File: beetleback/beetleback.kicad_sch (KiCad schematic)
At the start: 22 parts, among them J1 Conn_01x05_Female, J3 motor_pad_1, J4 motor_pad_2, Q1 IRF7351TRPBF, Q2 IRF7351TRPBF, U1 ATtiny13A-SS, U2 DRV8701P

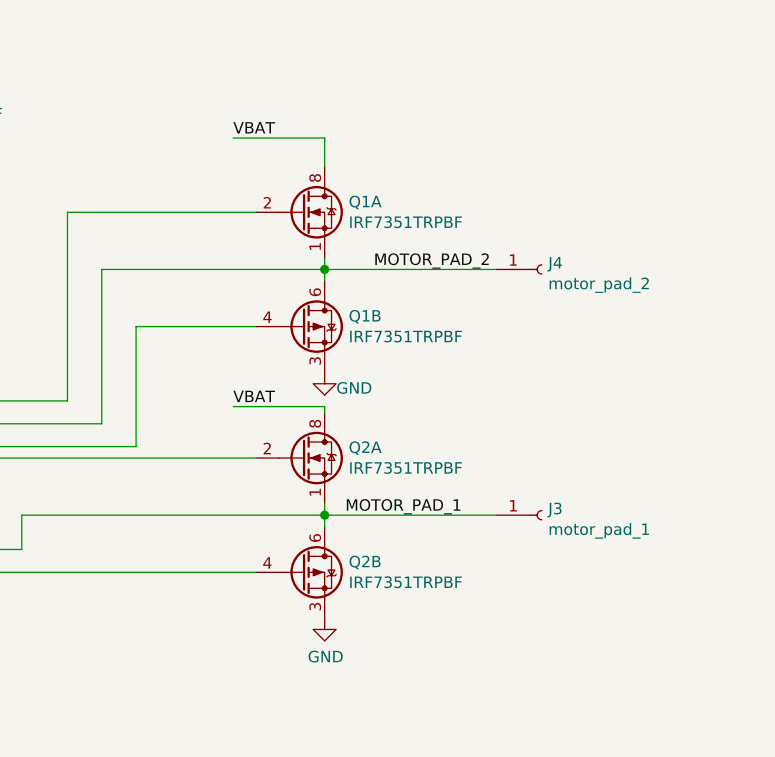
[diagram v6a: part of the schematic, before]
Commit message: Correct schematic booboo: use n-channel mosfets instead of a mixture
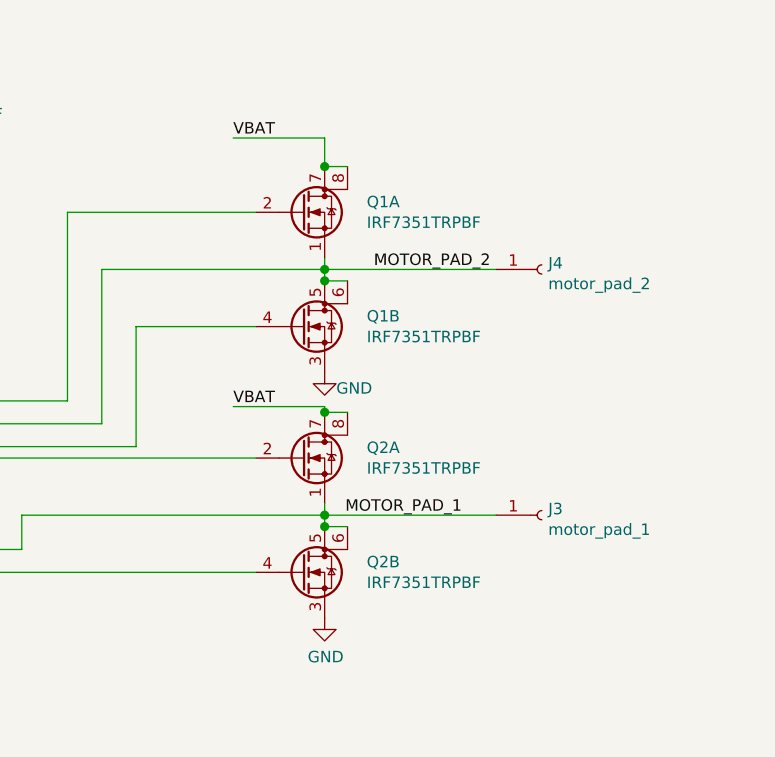
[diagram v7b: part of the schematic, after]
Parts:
- removed Q1, Q2: IRF7351TRPBF, Package_SO:SOIC-8_3.9x4.9mm_P1.27mm, symbol Transistor_FET:IRF7343PBF
- added Q1, Q2: IRF7351TRPBF, Package_SO:SOIC-8_3.9x4.9mm_P1.27mm, symbol Device:Q_Dual_NMOS_S1G1S2G2D2D2D1D1
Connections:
- net GH1: now also Q1.2 (G)
- net GH2: now also Q2.2 (G)
- net GL1: now also Q1.4 (G)
- net GL2: now also Q2.4 (G)
- net GND: now also Q1.3 (S), Q2.3 (S)
- net MOTOR_PAD_1: now also Q2.1 (S), Q2.5 (D), Q2.6 (D)
- net MOTOR_PAD_2: now also Q1.1 (S), Q1.5 (D), Q1.6 (D)
- net VBAT: now also Q1.7 (D), Q1.8 (D), Q2.7 (D), Q2.8 (D)
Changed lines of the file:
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@@
   (junction (at 172.72 87.63) (diameter 1.016) (color 0 0 0 0))
   (junction (at 196.85 103.505) (diameter 1.016) (color 0 0 0 0))
+  (junction (at 244.475 97.155) (diameter 1.016) (color 0 0 0 0))
   (junction (at 244.475 108.585) (diameter 1.016) (color 0 0 0 0))
+  (junction (at 244.475 109.855) (diameter 1.016) (color 0 0 0 0))
+  (junction (at 244.475 124.46) (diameter 1.016) (color 0 0 0 0))
   (junction (at 244.475 135.89) (diameter 1.016) (color 0 0 0 0))
+  (junction (at 244.475 137.16) (diameter 1.016) (color 0 0 0 0))
+  (no_connect (at 27.94 50.8))
   (no_connect (at 182.88 118.745))
-  (no_connect (at 27.94 50.8))
   (no_connect (at 182.88 147.955))
   (no_connect (at 178.435 66.04))
@@
     (stroke (width 0) (type solid) (color 0 0 0 0))
   )
+  (wire (pts (xy 244.475 97.155) (xy 247.015 97.155))
+    (stroke (width 0) (type solid) (color 0 0 0 0))
+  )
   (wire (pts (xy 244.475 107.315) (xy 244.475 108.585))
     (stroke (width 0) (type solid) (color 0 0 0 0))
@@
     (stroke (width 0) (type solid) (color 0 0 0 0))
   )
+  (wire (pts (xy 244.475 109.855) (xy 247.015 109.855))
+    (stroke (width 0) (type solid) (color 0 0 0 0))
+  )
   (wire (pts (xy 244.475 123.825) (xy 244.475 124.46))
     (stroke (width 0) (type solid) (color 0 0 0 0))
   )
+  (wire (pts (xy 244.475 124.46) (xy 247.015 124.46))
+    (stroke (width 0) (type solid) (color 0 0 0 0))
+  )
   (wire (pts (xy 244.475 134.62) (xy 244.475 135.89))
     (stroke (width 0) (type solid) (color 0 0 0 0))
@@
   )
   (wire (pts (xy 244.475 135.89) (xy 263.525 135.89))
+    (stroke (width 0) (type solid) (color 0 0 0 0))
+  )
+  (wire (pts (xy 244.475 137.16) (xy 247.015 137.16))
     (stroke (width 0) (type solid) (color 0 0 0 0))
   )
@@
     )
   )
-  (symbol (lib_id "Transistor_FET:IRF7343PBF") (at 241.935 102.235 0) (unit 1)
-    (in_bom yes) (on_board yes)
-    (property "Reference" "Q1" (id 0) (at 247.1421 101.0856 0)
-      (effects (font (size 1.27 1.27)) (justify left))
-    )
-    (property "Value" "IRF7351TRPBF" (id 1) (at 247.142 103.384 0)
-      (effects (font (size 1.27 1.27)) (justify left))
-    )
-    (property "Footprint" "Package_SO:SOIC-8_3.9x4.9mm_P1.27mm" (id 2) (at 247.015 104.14 0)
-      (effects (font (size 1.27 1.27)) (justify left) hide)
-    )
-    (property "Datasheet" "http://www.irf.com/product-info/datasheets/data/irf7343ipbf.pdf" (id 3) (at 244.475 102.235 0)
-      (effects (font (size 1.27 1.27)) (justify left) hide)
+  (symbol (lib_id "Graphic:Logo_Open_Hardware_Small") (at 186.69 23.495 0) (unit 1)
+    (in_bom yes) (on_board yes)
+    (property "Reference" "#LOGO1" (id 0) (at 186.69 16.51 0)
+      (effects (font (size 1.27 1.27)) hide)
+    )
+    (property "Value" "Logo_Open_Hardware_Small" (id 1) (at 186.69 29.21 0)
+      (effects (font (size 1.27 1.27)) hide)
+    )
+    (property "Footprint" "beetleback:bbb_logo" (id 2) (at 186.69 23.495 0)
+      (effects (font (size 1.27 1.27)) hide)
+    )
+    (property "Datasheet" "~" (id 3) (at 186.69 23.495 0)
+      (effects (font (size 1.27 1.27)) hide)
+    )
+  )
+  (symbol (lib_id "Device:Q_Dual_NMOS_S1G1S2G2D2D2D1D1") (at 241.935 102.235 0) (unit 1)
+    (in_bom yes) (on_board yes)
+    (property "Reference" "Q1" (id 0) (at 249.1487 101.0856 0)
+      (effects (font (size 1.27 1.27)) (justify left))
+    )
+    (property "Value" "IRF7351TRPBF" (id 1) (at 249.149 103.384 0)
+      (effects (font (size 1.27 1.27)) (justify left))
+    )
+    (property "Footprint" "Package_SO:SOIC-8_3.9x4.9mm_P1.27mm" (id 2) (at 247.015 102.235 0)
+      (effects (font (size 1.27 1.27)) hide)
+    )
+    (property "Datasheet" "~" (id 3) (at 247.015 102.235 0)
+      (effects (font (size 1.27 1.27)) hide)
     )
     (property "LCSC" "C68403" (id 4) (at 241.935 102.235 0)
@@
     )
   )
-  (symbol (lib_id "Transistor_FET:IRF7343PBF") (at 241.935 114.935 0) (unit 2)
-    (in_bom yes) (on_board yes)
-    (property "Reference" "Q1" (id 0) (at 247.1421 113.7856 0)
-      (effects (font (size 1.27 1.27)) (justify left))
-    )
-    (property "Value" "IRF7351TRPBF" (id 1) (at 247.1421 116.0843 0)
-      (effects (font (size 1.27 1.27)) (justify left))
-    )
-    (property "Footprint" "Package_SO:SOIC-8_3.9x4.9mm_P1.27mm" (id 2) (at 247.015 116.84 0)
-      (effects (font (size 1.27 1.27)) (justify left) hide)
-    )
-    (property "Datasheet" "http://www.irf.com/product-info/datasheets/data/irf7343ipbf.pdf" (id 3) (at 244.475 114.935 0)
-      (effects (font (size 1.27 1.27)) (justify left) hide)
-    )
-    (property "LCSC" "C68403" (id 4) (at 241.935 114.935 0)
-      (effects (font (size 1.27 1.27)) hide)
-    )
-  )
-  (symbol (lib_id "Transistor_FET:IRF7343PBF") (at 241.935 129.54 0) (unit 1)
-    (in_bom yes) (on_board yes)
-    (property "Reference" "Q2" (id 0) (at 247.1421 128.3906 0)
-      (effects (font (size 1.27 1.27)) (justify left))
-    )
-    (property "Value" "IRF7351TRPBF" (id 1) (at 247.142 130.689 0)
-      (effects (font (size 1.27 1.27)) (justify left))
-    )
-    (property "Footprint" "Package_SO:SOIC-8_3.9x4.9mm_P1.27mm" (id 2) (at 247.015 131.445 0)
-      (effects (font (size 1.27 1.27)) (justify left) hide)
-    )
-    (property "Datasheet" "http://www.irf.com/product-info/datasheets/data/irf7343ipbf.pdf" (id 3) (at 244.475 129.54 0)
-      (effects (font (size 1.27 1.27)) (justify left) hide)
+  (symbol (lib_id "Device:Q_Dual_NMOS_S1G1S2G2D2D2D1D1") (at 241.935 114.935 0) (unit 2)
+    (in_bom yes) (on_board yes)
+    (property "Reference" "Q1" (id 0) (at 249.1487 113.7856 0)
+      (effects (font (size 1.27 1.27)) (justify left))
+    )
+    (property "Value" "IRF7351TRPBF" (id 1) (at 249.149 116.084 0)
+      (effects (font (size 1.27 1.27)) (justify left))
+    )
+    (property "Footprint" "Package_SO:SOIC-8_3.9x4.9mm_P1.27mm" (id 2) (at 247.015 114.935 0)
+      (effects (font (size 1.27 1.27)) hide)
+    )
+    (property "Datasheet" "~" (id 3) (at 247.015 114.935 0)
+      (effects (font (size 1.27 1.27)) hide)
+    )
+  )
+  (symbol (lib_id "Device:Q_Dual_NMOS_S1G1S2G2D2D2D1D1") (at 241.935 129.54 0) (unit 1)
+    (in_bom yes) (on_board yes)
+    (property "Reference" "Q2" (id 0) (at 249.1487 128.3906 0)
+      (effects (font (size 1.27 1.27)) (justify left))
+    )
+    (property "Value" "IRF7351TRPBF" (id 1) (at 249.149 130.689 0)
+      (effects (font (size 1.27 1.27)) (justify left))
+    )
+    (property "Footprint" "Package_SO:SOIC-8_3.9x4.9mm_P1.27mm" (id 2) (at 247.015 129.54 0)
+      (effects (font (size 1.27 1.27)) hide)
+    )
+    (property "Datasheet" "~" (id 3) (at 247.015 129.54 0)
+      (effects (font (size 1.27 1.27)) hide)
     )
     (property "LCSC" "C68403" (id 4) (at 241.935 129.54 0)
@@
     )
   )
-  (symbol (lib_id "Transistor_FET:IRF7343PBF") (at 241.935 142.24 0) (unit 2)
-    (in_bom yes) (on_board yes)
-    (property "Reference" "Q2" (id 0) (at 247.1421 141.0906 0)
-      (effects (font (size 1.27 1.27)) (justify left))
-    )
-    (property "Value" "IRF7351TRPBF" (id 1) (at 247.1421 143.3893 0)
-      (effects (font (size 1.27 1.27)) (justify left))
-    )
-    (property "Footprint" "Package_SO:SOIC-8_3.9x4.9mm_P1.27mm" (id 2) (at 247.015 144.145 0)
-      (effects (font (size 1.27 1.27)) (justify left) hide)
-    )
-    (property "Datasheet" "http://www.irf.com/product-info/datasheets/data/irf7343ipbf.pdf" (id 3) (at 244.475 142.24 0)
-      (effects (font (size 1.27 1.27)) (justify left) hide)
-    )
-    (property "LCSC" "C68403" (id 4) (at 241.935 142.24 0)
-      (effects (font (size 1.27 1.27)) hide)
-    )
-  )
-  (symbol (lib_id "Graphic:Logo_Open_Hardware_Small") (at 186.69 23.495 0) (unit 1)
-    (in_bom yes) (on_board yes)
-    (property "Reference" "#LOGO1" (id 0) (at 186.69 16.51 0)
-      (effects (font (size 1.27 1.27)) hide)
-    )
-    (property "Value" "Logo_Open_Hardware_Small" (id 1) (at 186.69 29.21 0)
-      (effects (font (size 1.27 1.27)) hide)
-    )
-    (property "Footprint" "beetleback:bbb_logo" (id 2) (at 186.69 23.495 0)
-      (effects (font (size 1.27 1.27)) hide)
-    )
-    (property "Datasheet" "~" (id 3) (at 186.69 23.495 0)
+  (symbol (lib_id "Device:Q_Dual_NMOS_S1G1S2G2D2D2D1D1") (at 241.935 142.24 0) (unit 2)
+    (in_bom yes) (on_board yes)
+    (property "Reference" "Q2" (id 0) (at 249.1487 141.0906 0)
+      (effects (font (size 1.27 1.27)) (justify left))
+    )
+    (property "Value" "IRF7351TRPBF" (id 1) (at 249.149 143.389 0)
+      (effects (font (size 1.27 1.27)) (justify left))
+    )
+    (property "Footprint" "Package_SO:SOIC-8_3.9x4.9mm_P1.27mm" (id 2) (at 247.015 142.24 0)
+      (effects (font (size 1.27 1.27)) hide)
+    )
+    (property "Datasheet" "~" (id 3) (at 247.015 142.24 0)
       (effects (font (size 1.27 1.27)) hide)
     )
@@
       (reference "J4") (unit 1) (value "motor_pad_2") (footprint "beetleback:bbb_motorpin")
     )
-    (path "/0f33e45a-ef24-4ac4-83eb-7cf104015784"
+    (path "/a69a273c-4e3e-46dc-8062-8d9f361d07d3"
       (reference "Q1") (unit 1) (value "IRF7351TRPBF") (footprint "Package_SO:SOIC-8_3.9x4.9mm_P1.27mm")
     )
-    (path "/bf41a1ad-5460-44cc-b329-1c158f60a46d"
+    (path "/86cb0b69-ddbd-42cc-8e88-2d4ebc15451c"
       (reference "Q1") (unit 2) (value "IRF7351TRPBF") (footprint "Package_SO:SOIC-8_3.9x4.9mm_P1.27mm")
     )
-    (path "/40ea8a05-4afc-4962-9870-9910f719101e"
+    (path "/d094f7e5-7051-4491-9470-d138e254b828"
       (reference "Q2") (unit 1) (value "IRF7351TRPBF") (footprint "Package_SO:SOIC-8_3.9x4.9mm_P1.27mm")
     )
-    (path "/23f89606-4f0f-4a94-8596-a6b3669b94fd"
+    (path "/fdf323e3-1e06-45a9-b347-9010497d9e39"
       (reference "Q2") (unit 2) (value "IRF7351TRPBF") (footprint "Package_SO:SOIC-8_3.9x4.9mm_P1.27mm")
     )

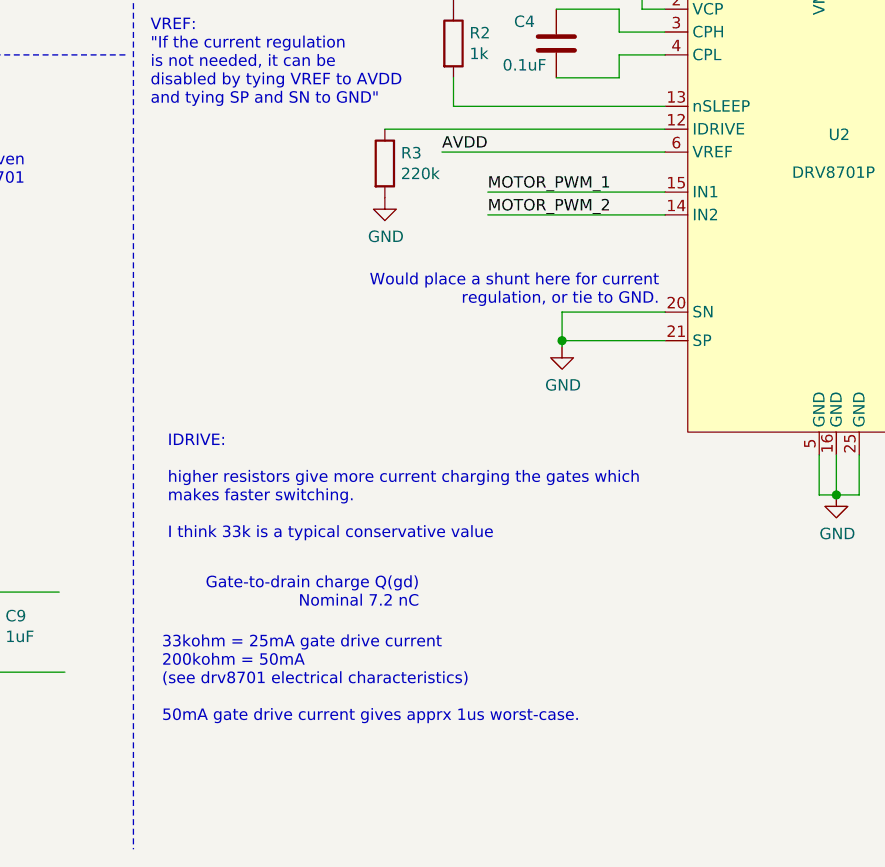
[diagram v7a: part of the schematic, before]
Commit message: more copper under fets, r3 dnp 0603
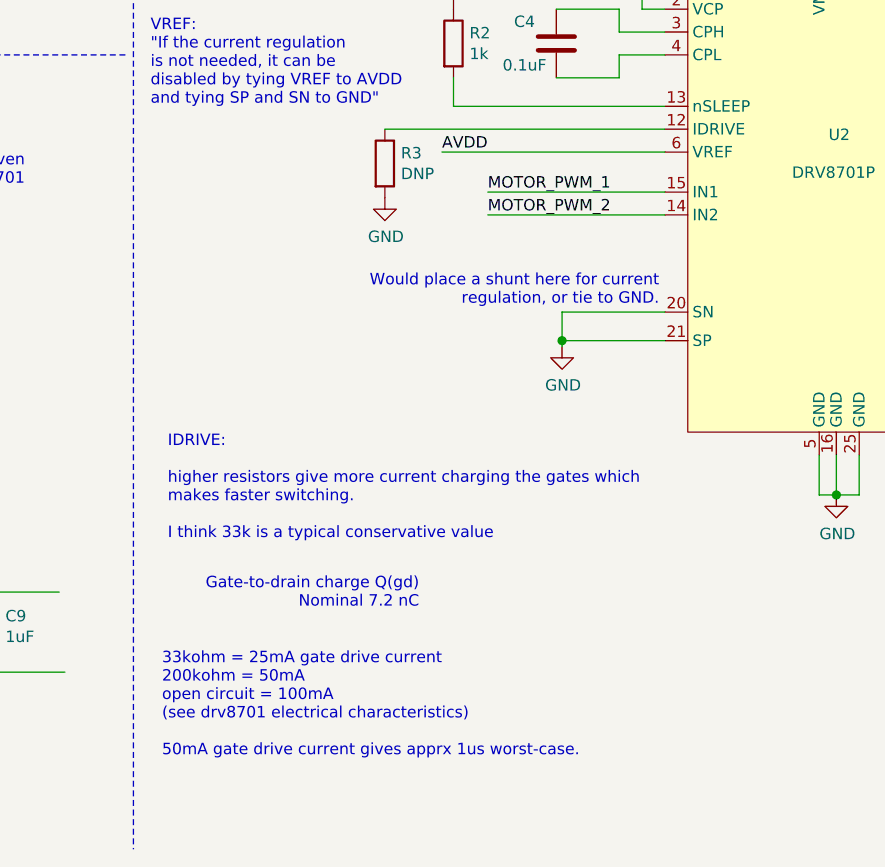
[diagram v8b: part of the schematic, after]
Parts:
- R3: value 220k -> DNP; footprint Resistor_SMD:R_0402_1005Metric -> Resistor_SMD:R_0603_1608Metric; LCSC C25767 -> (none)
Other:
- note added: "33kohm = 25mA gate drive current 200kohm = 50mA open circuit = 100mA (see drv8701 electrical characteristics) 50mA gate drive current gives apprx 1us worst-case."
- note removed: "33kohm = 25mA gate drive current 200kohm = 50mA (see drv8701 electrical characteristics) 50mA gate drive current gives apprx 1us worst-case."
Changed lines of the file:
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@@
   (junction (at 244.475 135.89) (diameter 1.016) (color 0 0 0 0))
   (junction (at 244.475 137.16) (diameter 1.016) (color 0 0 0 0))
+  (no_connect (at 182.88 147.955))
+  (no_connect (at 182.88 118.745))
+  (no_connect (at 178.435 66.04))
   (no_connect (at 27.94 50.8))
-  (no_connect (at 182.88 118.745))
-  (no_connect (at 182.88 147.955))
-  (no_connect (at 178.435 66.04))
   (wire (pts (xy 18.415 170.18) (xy 24.13 170.18))
     (stroke (width 0) (type solid) (color 0 0 0 0))
@@
     (effects (font (size 1.27 1.27)) (justify left bottom))
   )
-  (text "33kohm = 25mA gate drive current\n200kohm = 50mA\n(see drv8701 electrical characteristics)\n\n50mA gate drive current gives apprx 1us worst-case."
-    (at 88.265 184.785 0)
+  (text "33kohm = 25mA gate drive current\n200kohm = 50mA\nopen circuit = 100mA\n(see drv8701 electrical characteristics)\n\n50mA gate drive current gives apprx 1us worst-case."
+    (at 88.265 188.595 0)
     (effects (font (size 1.27 1.27)) (justify left bottom))
   )
@@
       (effects (font (size 1.27 1.27)) (justify left))
     )
-    (property "Value" "220k" (id 1) (at 114.808 123.704 0)
-      (effects (font (size 1.27 1.27)) (justify left))
-    )
-    (property "Footprint" "Resistor_SMD:R_0402_1005Metric" (id 2) (at 111.252 122.555 90)
+    (property "Value" "DNP" (id 1) (at 114.808 123.704 0)
+      (effects (font (size 1.27 1.27)) (justify left))
+    )
+    (property "Footprint" "Resistor_SMD:R_0603_1608Metric" (id 2) (at 111.252 122.555 90)
       (effects (font (size 1.27 1.27)) hide)
     )
@@
       (effects (font (size 1.27 1.27)) hide)
     )
-    (property "LCSC" "C25767" (id 4) (at 113.03 122.555 0)
+    (property "LCSC" "" (id 4) (at 113.03 122.555 0)
       (effects (font (size 1.27 1.27)) hide)
     )
@@
     )
     (path "/96fca56c-a1c6-47bb-9c21-6e480b894a8c"
-      (reference "R3") (unit 1) (value "220k") (footprint "Resistor_SMD:R_0402_1005Metric")
+      (reference "R3") (unit 1) (value "DNP") (footprint "Resistor_SMD:R_0603_1608Metric")
     )
     (path "/1f054975-e5a8-442f-b188-82daf3387f2d"
